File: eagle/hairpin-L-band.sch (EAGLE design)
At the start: 14 parts, among them J1 142-0701-851_TEST, J2 142-0701-851_TEST

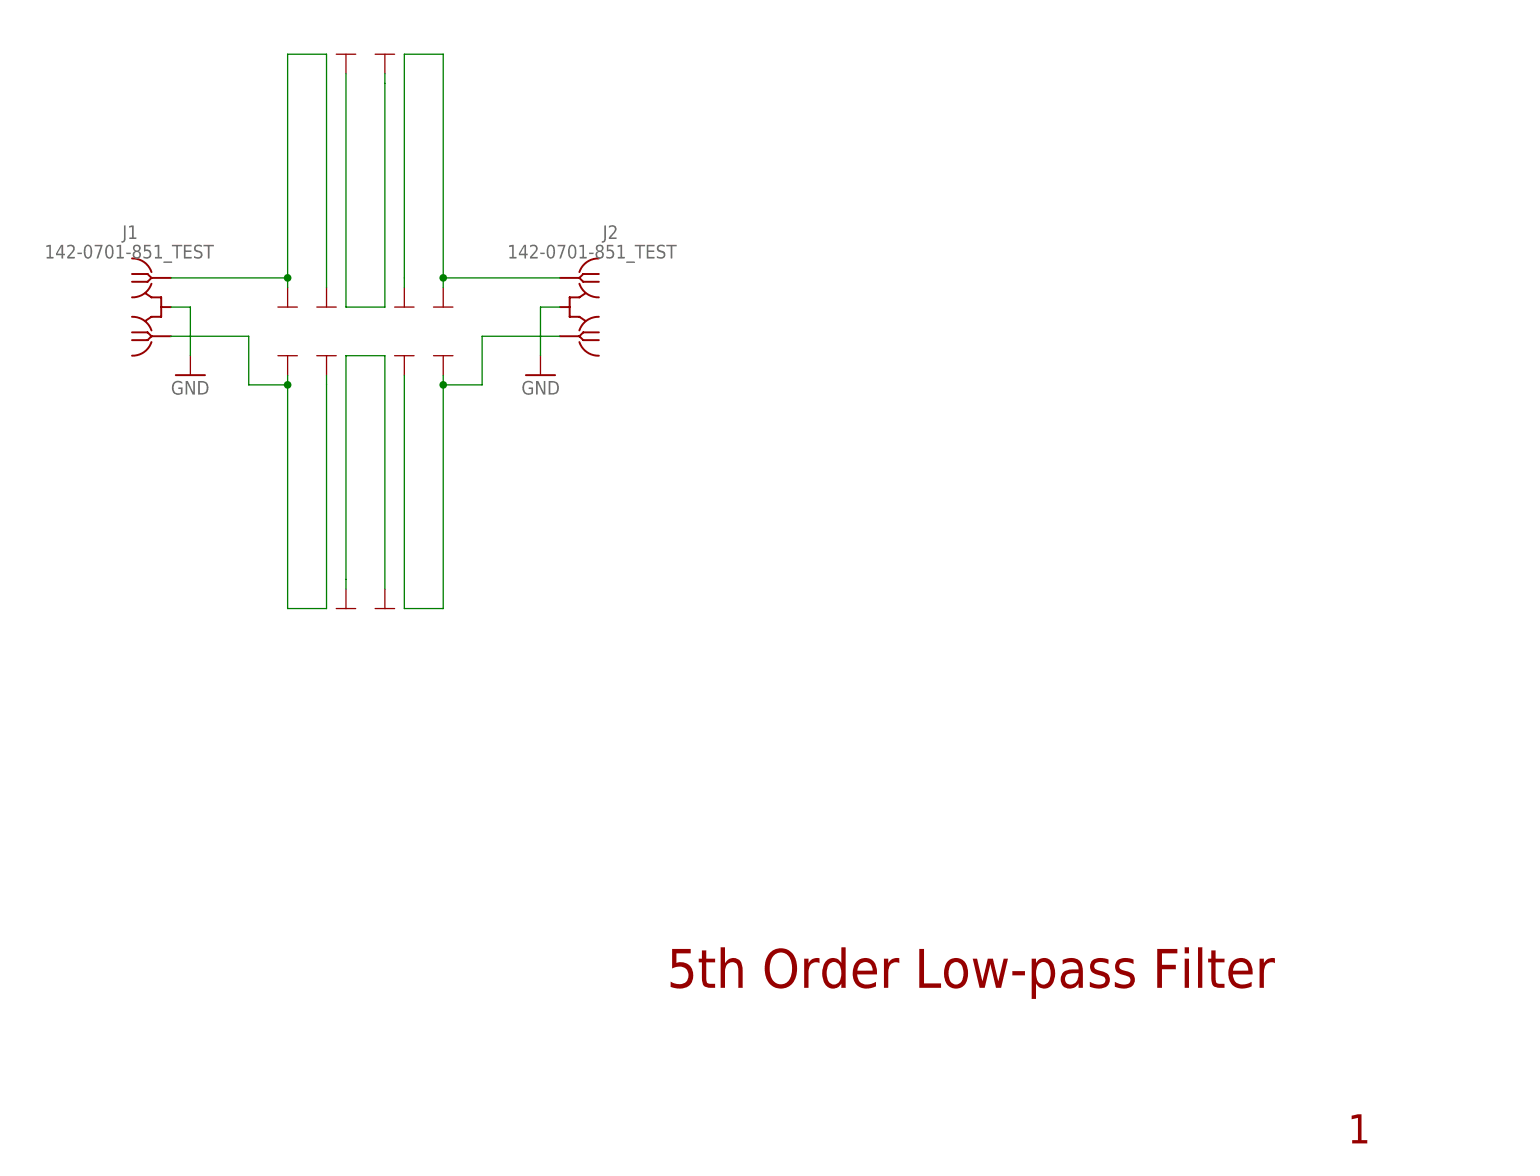
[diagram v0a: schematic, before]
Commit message: Update L band hairpin
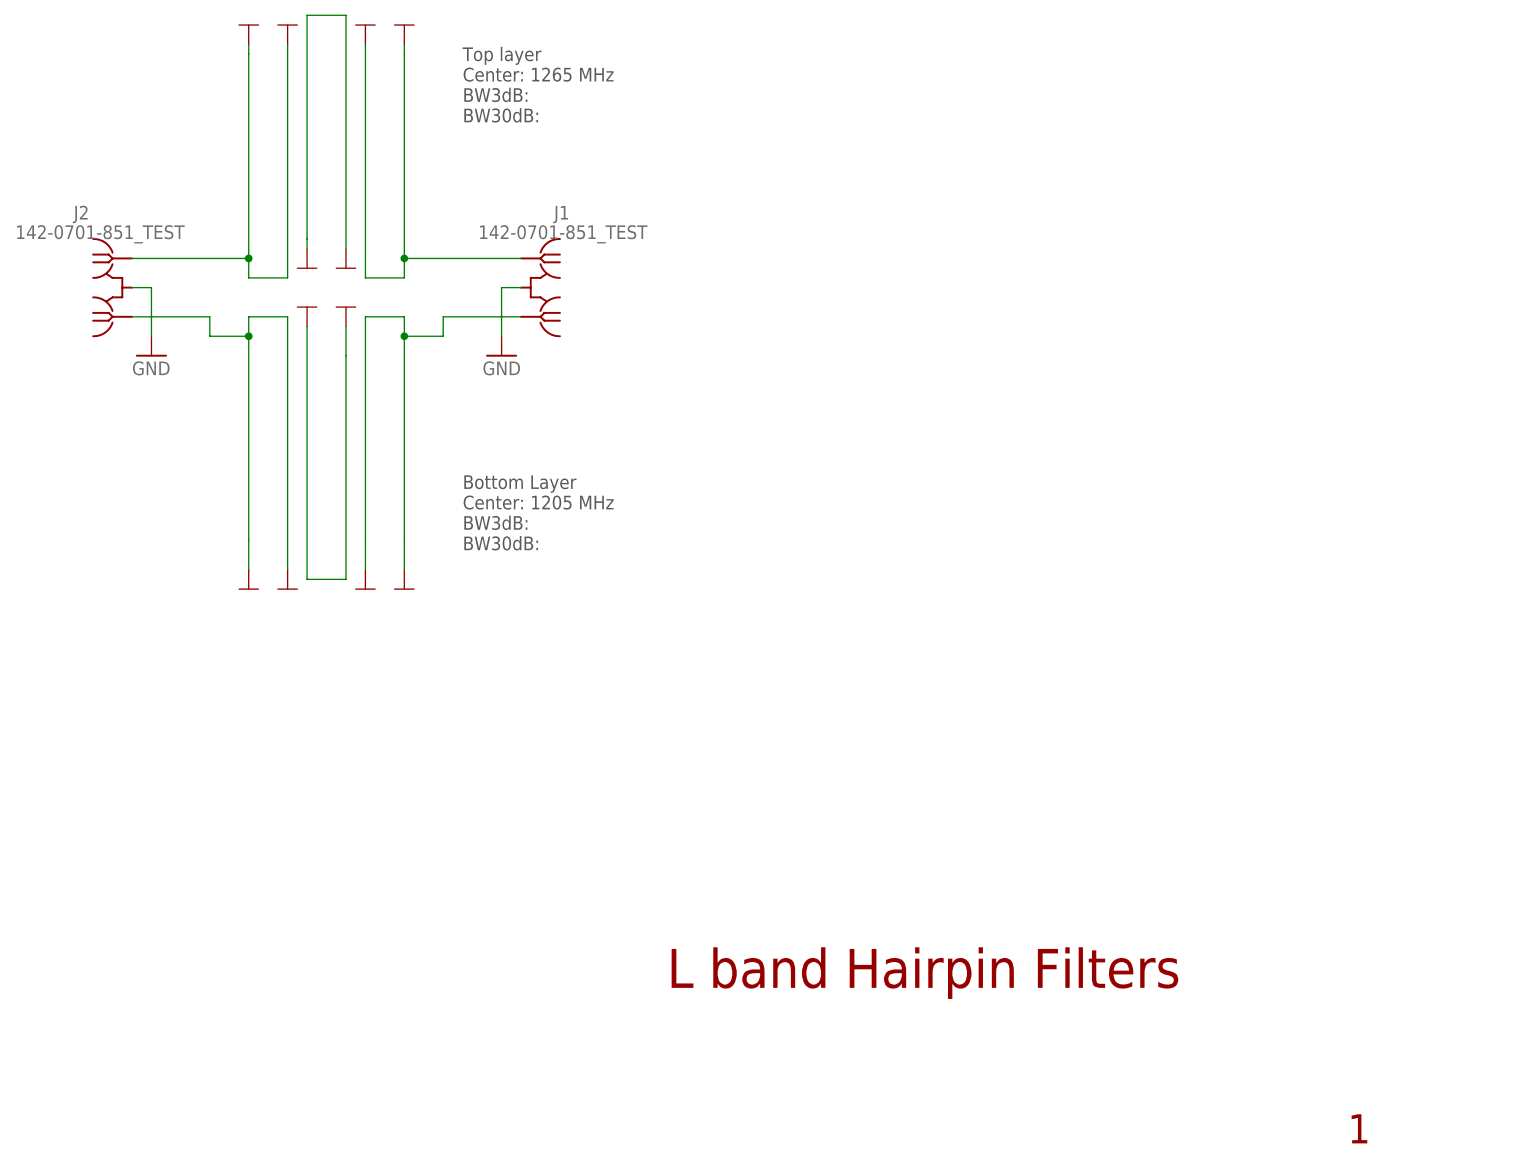
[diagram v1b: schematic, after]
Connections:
- net BLEFT: now also J2.RF2, U$11.END, U$12.END; no longer J1.RF2, U$7.END, U$8.END
- net BRIGHT: now also J1.RF2, U$7.END, U$8.END; no longer J2.RF2, U$11.END, U$12.END
- net TLEFT: now also J2.RF1, U$5.END, U$6.END; no longer J1.RF1, U$1.END, U$2.END
- net TRIGHT: now also J1.RF1, U$1.END, U$2.END; no longer J2.RF1, U$5.END, U$6.END
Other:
- note added: "Bottom Layer Center: 1205 MHz BW3dB: BW30dB:"
- note added: "L band Hairpin Filters"
- note added: "Top layer Center: 1265 MHz BW3dB: BW30dB:"
- note removed: "5th Order Low-pass Filter"
- moved on the sheet: J1, J2
